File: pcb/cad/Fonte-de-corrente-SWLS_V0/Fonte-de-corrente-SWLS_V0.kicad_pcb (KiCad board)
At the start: 2 copper layers, 32 parts, among them J2 LEMO FFA.0S, J3 LEMO FFA.0S, J4 Barrel_Jack_Switch, SW1 SW_DIP_x01, U1 LM7805, U2 LT3080xST, U3 LT3092xST, U4 LT3092xST, U5 74AHC1G04, U6 TS5A21366, U7 TS5A21366, U8 TS5A21366, U9 TS5A21366

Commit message: Atualização do layout da PCB
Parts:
- added C10: 0.1uF, Capacitor_SMD:C_0805_2012Metric, F.Cu at (21.0, 58.4)
- R1, R2: value 1MR -> 1M
- R4, R5: value 100R -> 100
- R6, R7: value 22KR -> 22K
- R8, R9: value 120R -> 120
- SW1: footprint Button_Switch_THT:SW_DIP_SPSTx01_Piano_10.8x4.1mm_W7.62mm_P2.54mm -> Fonte-de-corrente-SWLS-complementar:Chave analógica; moved to F.Cu
- U1: value LM7805 -> LM78L05
- moved R2 19.5 mm to (15.6, 50.4), turned to -90 degrees
- moved J3 18.6 mm to (53.7, 60.0)
- moved J2 17.9 mm to (53.2, 40.6), turned to -90 degrees
- moved R1 16.4 mm to (18.5, 50.4), turned to -90 degrees
- moved C1 14.2 mm to (18.4, 53.9)
- moved SW1 10.6 mm to (30.8, 71.8)
- moved C4 9.71 mm to (16.9, 67.6), turned to 180 degrees
- moved C8 7.92 mm to (53.1, 53.2)
- moved C2 6.68 mm to (16.7, 59.2)
- moved R9 5.70 mm to (38.1, 52.4), turned to 0 degrees
- moved U8 5.50 mm to (49.3, 40.6), turned to 90 degrees
- moved R5 5.49 mm to (33.9, 52.4)
- moved U7 5.33 mm to (44.5, 40.5), turned to 90 degrees
- moved U1 5.17 mm to (17.8, 61.8), turned to -90 degrees
- moved C9 4.44 mm to (53.5, 66.7)
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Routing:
- net GND: track 0.00 -> 12.1 mm
- net /CH2+: track 0.00 -> 7.30 mm
- net /CH2-: track 0.00 -> 7.00 mm
- net /1mADC_CH2: track 0.00 -> 6.35 mm

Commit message: Atualização do layout de PCB
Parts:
- moved C10 32.1 mm to (52.5, 51.9), turned to 180 degrees
- moved C4 29.2 mm to (40.5, 50.4), turned to -90 degrees
- moved U5 28.6 mm to (52.3, 48.9)
- moved R3 25.3 mm to (43.3, 50.5), turned to 90 degrees
- moved SW1 22.0 mm to (40.6, 52.0), turned to 90 degrees
- moved U1 21.2 mm to (35.1, 49.7), turned to 0 degrees
- moved C5 20.5 mm to (17.8, 57.8), turned to 0 degrees
- moved C2 15.3 mm to (29.5, 50.8), turned to -90 degrees
- moved R2 14.5 mm to (29.5, 54.6), turned to 90 degrees
- moved C8 12.0 mm to (44.7, 61.8)
- moved U8 9.01 mm to (40.4, 39.2), turned to 0 degrees
- moved R1 8.90 mm to (26.4, 54.5), turned to 90 degrees
- moved C1 8.56 mm to (26.4, 50.8), turned to -90 degrees
- moved R7 7.35 mm to (37.1, 60.4)
- moved U4 7.35 mm to (30.7, 64.5)
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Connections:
- R3 pad 2: Net-(R3-Pad2) -> /IN
- SW1 pad 2: Net-(R3-Pad2) -> /IN
- U6 pad 1: /1mADC_CH2 -> /CH2+
- U6 pad 2: /CH2+ -> /1mADC_CH2
- U6 pad 3: /~{IN} -> /IN
- U6 pad 6: /CH2+ -> /CH2-
- U7 pad 1: /1mADC_CH1 -> /CH1+
- U7 pad 2: /CH1+ -> /1mADC_CH1
- U8 pad 5: /1mADC_CH1 -> /CH1-
- U8 pad 6: /CH1- -> /1mADC_CH1
- U9 pad 1: /1mADC_CH2 -> GND
- U9 pad 2: /CH2- -> /CH2+
- U9 pad 3: /IN -> /~{IN}
- U9 pad 5: GND -> /CH2-
- U9 pad 6: /CH2- -> /1mADC_CH2
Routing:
- net /5V_REG: track 0.00 -> 57.0 mm
- net /~{IN}: track 0.00 -> 46.8 mm
- net /IN: track 0.00 -> 43.2 mm
- net /VIN: track 0.00 -> 20.8 mm
- net GND: track 12.1 -> 29.8 mm
- net +5V: track 0.00 -> 17.7 mm
- net /1mADC_CH1: track 0.00 -> 14.9 mm
- net /CH1-: track 0.00 -> 10.8 mm
- net /1mADC_CH2: track 6.35 -> 16.8 mm
- net /CH1+: track 0.00 -> 10.3 mm
- net Net-(R4-Pad1): track 0.00 -> 10.1 mm
- net Net-(R5-Pad1): track 0.00 -> 9.89 mm
- net Net-(U2-SET): track 0.00 -> 6.23 mm
- net /CH2-: track 7.00 -> 11.2 mm
- net Net-(R7-Pad1): track 0.00 -> 4.06 mm
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
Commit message: Atualização do layout de PCB
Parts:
- moved C3 5.26 mm to (23.2, 47.2), turned to 180 degrees
- moved R6 4.93 mm to (33.3, 35.2)
- moved R7 4.45 mm to (33.3, 58.2)
- moved R9 3.33 mm to (30.7, 58.2), turned to 90 degrees
- moved R8 3.21 mm to (30.4, 35.1), turned to -90 degrees
- moved C7 3.10 mm to (40.9, 38.3)
- moved C6 3.10 mm to (48.0, 38.3)
- moved U7 3.10 mm to (44.6, 38.2)
- moved U8 3.10 mm to (37.5, 38.1)
- moved U6 2.95 mm to (45.3, 61.2)
- moved U9 2.95 mm to (38.4, 61.2)
- moved C8 2.95 mm to (41.8, 61.5)
- moved C9 2.95 mm to (48.9, 61.1)
- moved J3 2.95 mm to (52.1, 61.4)
- moved J2 2.80 mm to (51.1, 38.1)
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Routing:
- net /~{IN}: track 46.8 -> 6.61 mm
- net /IN: track 43.2 -> 7.57 mm
- net /CH2+: track 9.46 -> 39.0 mm
- net /5V_REG: track 57.0 -> 45.2 mm
- net /CH1+: track 10.3 -> 21.2 mm
- net GND: track 29.8 -> 20.2 mm
- net /1mADC_CH2: track 16.8 -> 8.17 mm
- net /CH1-: track 10.8 -> 18.6 mm
- net /1mADC_CH1: track 14.9 -> 8.48 mm
- net /VIN: track 20.8 -> 25.1 mm
- net Net-(R7-Pad1): track 4.06 -> 0.00 mm
- net Net-(R6-Pad1): track 3.96 -> 0.00 mm
- net Net-(R5-Pad1): track 9.89 -> 6.30 mm
- net /CH2-: track 11.2 -> 14.4 mm
- net Net-(R4-Pad1): track 10.1 -> 7.60 mm
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- added copper zone on F.Cu, net GND
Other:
- board outline added: 59.9 x 38 mm

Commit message: Atualização do layout de PCB
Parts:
- J2, J3: footprint Fonte-de-corrente-SWLS-complementar:Lemo_Painel_4vias -> Fonte-de-corrente-SWLS-complementar:EPG.0B.302.HLN; moved to B.Cu
- SW1: value SW_DIP_x01 -> SW_DPDT_x2; footprint Fonte-de-corrente-SWLS-complementar:Chave analógica -> Fonte-de-corrente-SWLS-complementar:SW_100SP1T2B4M6QE; moved to B.Cu
- moved C10 36.3 mm to (26.4, 77.1)
- moved U5 36.3 mm to (26.2, 74.1)
- moved R5 23.1 mm to (35.4, 80.1)
- moved R7 23.1 mm to (40.6, 80.1)
- moved R9 23.1 mm to (38.1, 80.1)
- moved U4 23.1 mm to (38.1, 86.5)
- moved R3 20.5 mm to (23.5, 55.7), turned to -90 degrees
- moved R2 18.4 mm to (47.9, 55.6)
- moved C2 18.4 mm to (47.9, 51.8)
- moved U2 18.4 mm to (38.7, 53.7)
- moved C1 18.4 mm to (44.8, 51.9)
- moved C5 18.4 mm to (34.5, 58.8)
- moved R1 18.4 mm to (44.8, 55.6)
- moved J2 15.5 mm to (66.1, 41.9), turned to 0 degrees
- moved SW1 14.9 mm to (27.1, 58.2), turned to -90 degrees
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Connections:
- SW1 pad 1: GND -> +5V
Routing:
- net /5V_REG: track 45.2 -> 11.4 mm
- net /VIN: track 25.1 -> 10.6 mm

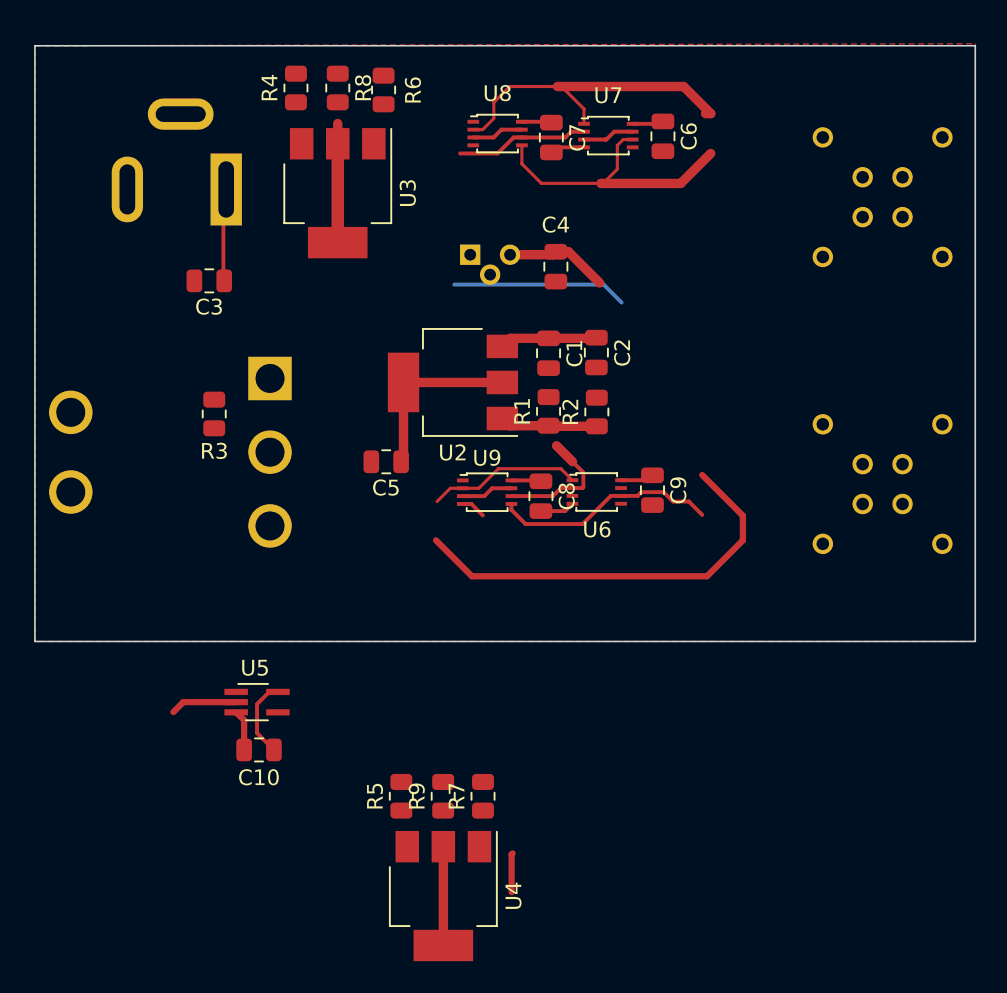
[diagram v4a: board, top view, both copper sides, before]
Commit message: Atualização do layout de PCB para revisão
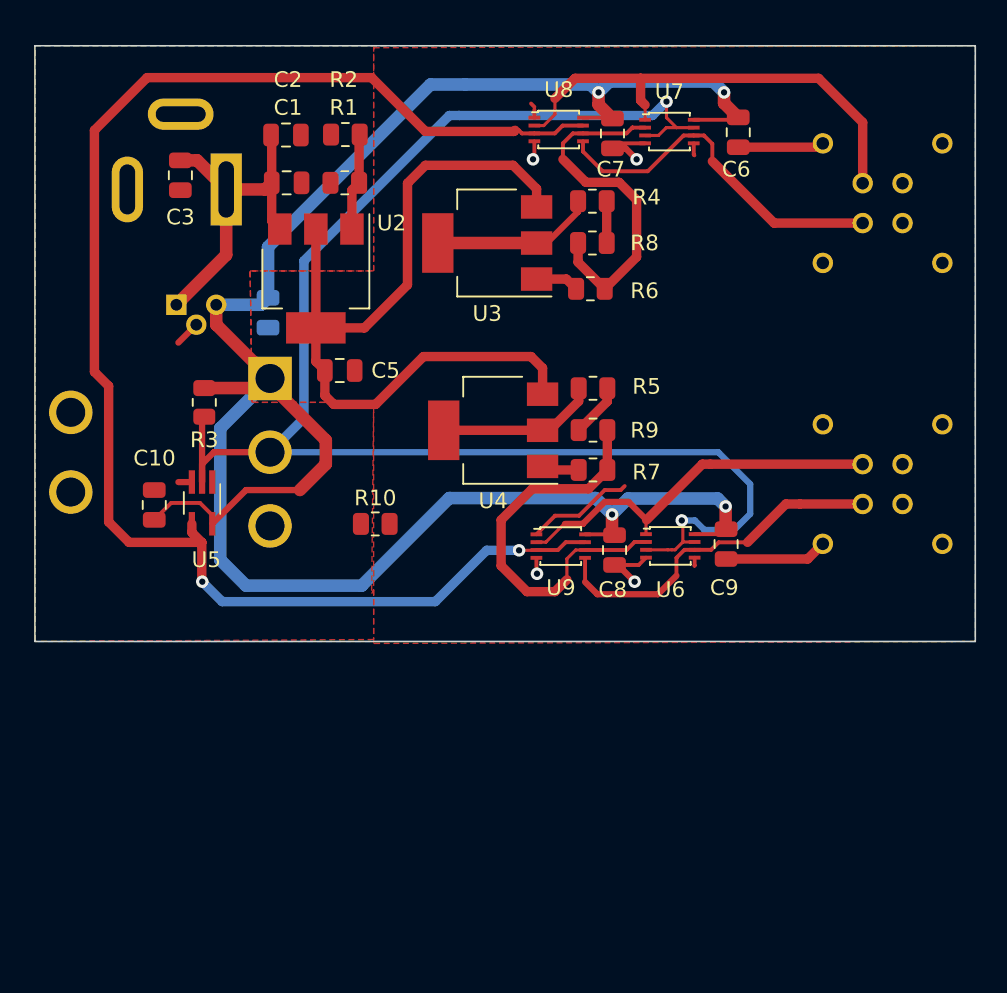
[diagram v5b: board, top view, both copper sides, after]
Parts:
- removed REF**: Lemo Painel, Lemo Painel
- added R10: 0, Resistor_SMD:R_0805_2012Metric, F.Cu at (33.8, 62.7)
- C4: moved to B.Cu
- moved U4 29.9 mm to (41.3, 56.8), turned to 180 degrees
- moved R5 28.7 mm to (47.6, 54.1), turned to 0 degrees
- moved R9 25.2 mm to (47.6, 56.8), turned to 0 degrees
- moved C2 24.2 mm to (28.1, 37.9), turned to 0 degrees
- moved R2 23.9 mm to (31.9, 37.9), turned to 180 degrees
- moved R7 22.0 mm to (47.6, 59.3), turned to 0 degrees
- moved R4 20.2 mm to (47.6, 42.2), turned to 0 degrees
- moved C1 19.9 mm to (28.1, 41.0), turned to 0 degrees
- moved R1 19.5 mm to (31.8, 41.0), turned to 180 degrees
- moved R8 19.0 mm to (47.6, 44.8), turned to 180 degrees
- moved U1 19.0 mm to (21.1, 48.8)
- moved C4 18.6 mm to (26.9, 49.3)
- moved R6 18.3 mm to (47.5, 47.8), turned to 0 degrees
- moved C10 17.0 mm to (19.7, 61.5), turned to 90 degrees
- moved U5 13.2 mm to (22.7, 61.4), turned to -90 degrees
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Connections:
- C5 pad 2: GND -> GNDA
- J2 pad 3: (no net) -> unconnected-(J2-Pad3)
- J2 pad 5: (no net) -> GND
- J2 pad 6: (no net) -> GND
- J2 pad 7: (no net) -> GND
- J2 pad 8: (no net) -> GND
- J3 pad 3: (no net) -> unconnected-(J3-Pad3)
- J3 pad 5: (no net) -> GND
- J3 pad 6: (no net) -> GND
- J3 pad 7: (no net) -> GND
- J3 pad 8: (no net) -> GND
- SW1 pad S1: (no net) -> GND
- SW1 pad S2: (no net) -> GND
- U6 pad 5: GND -> GNDA
- U7 pad 5: GND -> GNDA
- U8 pad 1: GND -> GNDA
- U9 pad 1: GND -> GNDA
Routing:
- net +5V: track 19.6 -> 137.0 mm, vias 0 -> 4
- net /IN: track 7.57 -> 98.7 mm, vias 0 -> 2
- net /~{IN}: track 6.61 -> 96.6 mm, vias 0 -> 2
- net /5V_REG: track 11.4 -> 52.1 mm
- net /1mADC_CH2: track 8.17 -> 25.6 mm
- net /CH2+: track 39.0 -> 24.7 mm
- net /1mADC_CH1: track 8.48 -> 22.6 mm
- net /VIN: track 10.6 -> 21.7 mm
- net /CH1+: track 21.2 -> 30.6 mm
- net GNDA: track 0.00 -> 9.03 mm
- net /CH2-: track 14.4 -> 22.6 mm
- net GND: track 20.2 -> 24.7 mm, vias 0 -> 4
- net /CH1-: track 18.6 -> 22.9 mm
- net Net-(R5-Pad1): track 6.30 -> 10.2 mm
- net Net-(R5-Pad2): track 0.00 -> 3.42 mm
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- added copper zone on B.Cu, net GND
- added copper zone on F.Cu, net GNDA

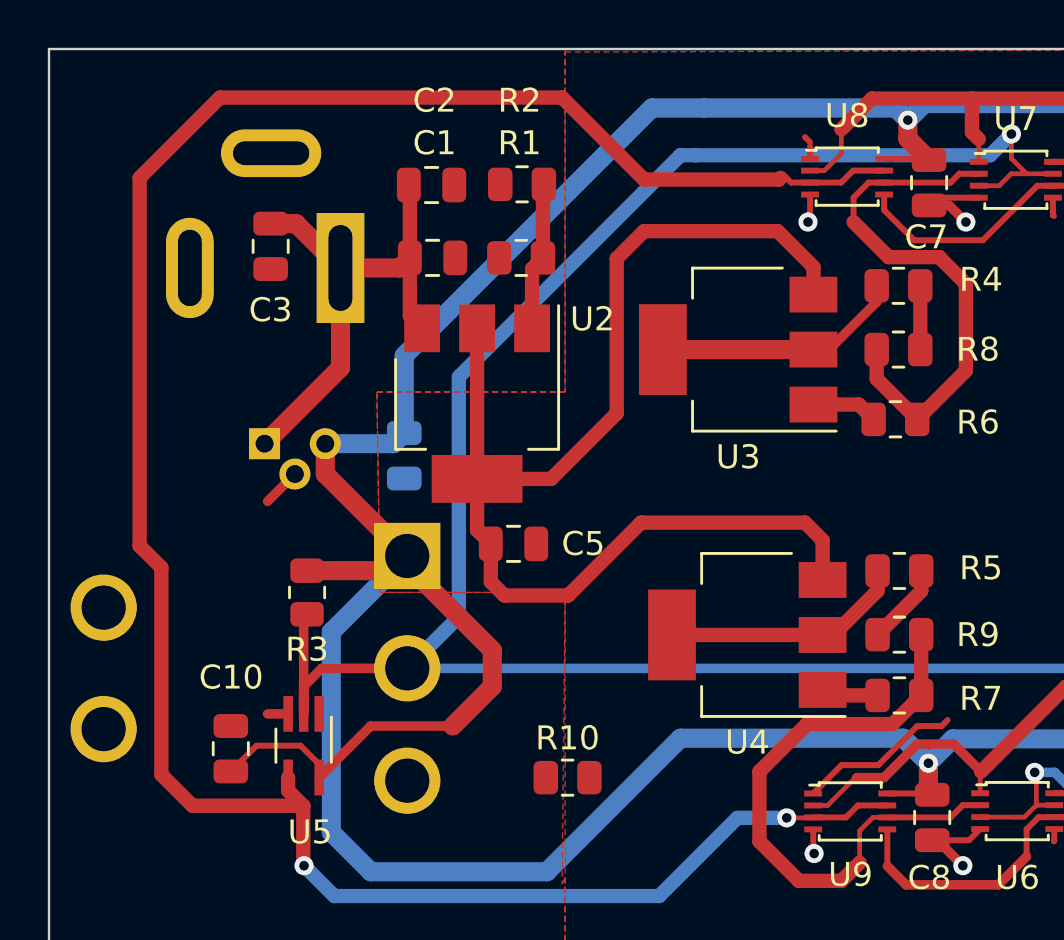
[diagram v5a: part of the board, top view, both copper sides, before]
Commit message: Atualização do layout de PCB com as correções indicadas nas issues
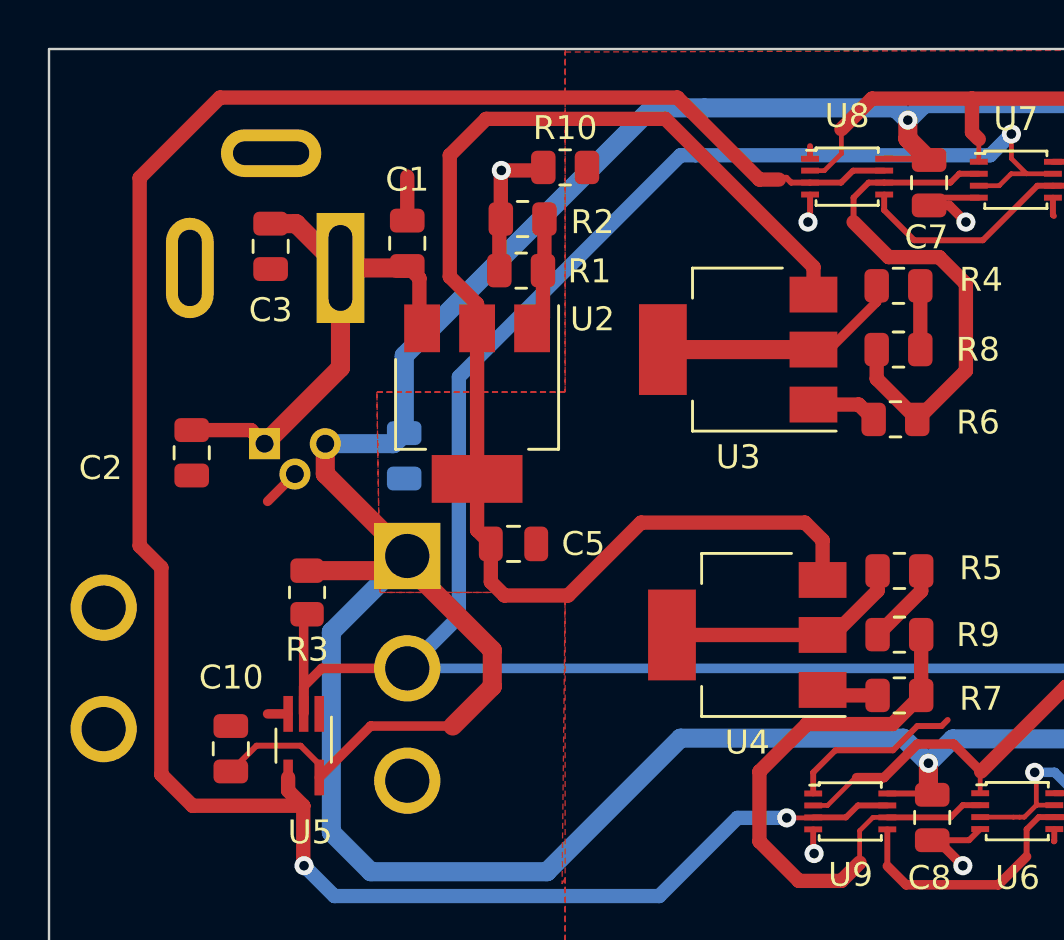
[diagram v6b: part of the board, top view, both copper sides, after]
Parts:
- moved R10 25.5 mm to (33.7, 37.2)
- moved C2 15.0 mm to (18.0, 49.1), turned to -90 degrees
- moved R2 1.45 mm to (31.9, 39.4)
- moved C1 1.22 mm to (27.1, 40.4), turned to 90 degrees
- moved R1 0.53 mm to (31.8, 41.5)
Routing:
- net GND: track 24.7 -> 32.6 mm, vias 4 -> 5
- net /5V_REG: track 52.1 -> 55.5 mm
- net Net-(U2-SET): track 6.23 -> 4.79 mm

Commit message: Atualização do layout de PCB e esquemático com as correções indicadas nas issues
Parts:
- C5: value 2.2uF -> 10uF
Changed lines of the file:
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@@
         (effects (font (size 1 1) (thickness 0.15)))
     )
-    (fp_text value "2.2uF" (at 0 1.68) (layer "F.Fab")
+    (fp_text value "10uF" (at 0 1.68) (layer "F.Fab")
         (effects (font (size 1 1) (thickness 0.15)))
     )
